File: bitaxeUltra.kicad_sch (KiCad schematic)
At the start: 16 parts, among them J1 54-00164

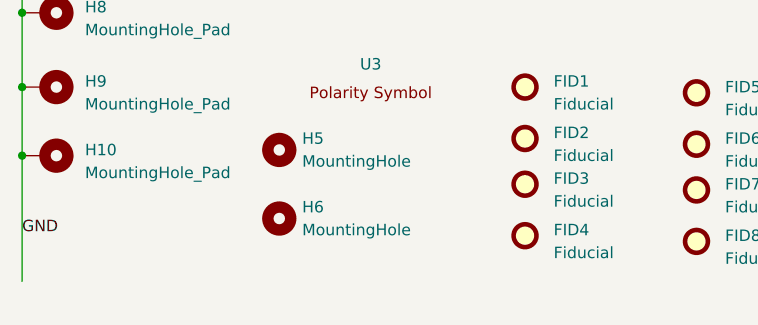
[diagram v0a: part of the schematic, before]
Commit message: added sda and scl puulups
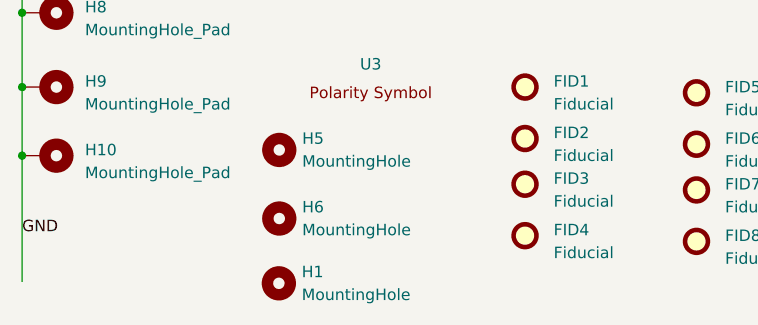
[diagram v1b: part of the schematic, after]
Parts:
- added H1: MountingHole, MountingHole:MountingHole_3.5mm, symbol Mechanical:MountingHole
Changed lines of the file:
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@@
+	)
+	(symbol
+		(lib_id "Mechanical:MountingHole")
+		(at 63.4535 193.2552 0)
+		(unit 1)
+		(exclude_from_sim no)
+		(in_bom no)
+		(on_board yes)
+		(dnp no)
+		(fields_autoplaced yes)
+		(property "Reference" "H1"
+			(at 65.9935 191.9851 0)
+			(effects
+				(font
+					(size 1.27 1.27)
+				)
+				(justify left)
+			)
+		)
+		(property "Value" "MountingHole"
+			(at 65.9935 194.5251 0)
+			(effects
+				(font
+					(size 1.27 1.27)
+				)
+				(justify left)
+			)
+		)
+		(property "Footprint" "MountingHole:MountingHole_3.5mm"
+			(at 63.4535 193.2552 0)
+			(effects
+				(font
+					(size 1.27 1.27)
+				)
+				(hide yes)
+			)
+		)
+		(property "Datasheet" "~"
+			(at 63.4535 193.2552 0)
+			(effects
+				(font
+					(size 1.27 1.27)
+				)
+				(hide yes)
+			)
+		)
+		(property "Description" ""
+			(at 63.4535 193.2552 0)
+			(effects
+				(font
+					(size 1.27 1.27)
+				)
+				(hide yes)
+			)
+		)
+		(instances
+			(project "bitaxeUltra"
+				(path "/e63e39d7-6ac0-4ffd-8aa3-1841a4541b55"
+					(reference "H1")
+					(unit 1)
+				)
+			)
+		)
 	)
 	(symbol
